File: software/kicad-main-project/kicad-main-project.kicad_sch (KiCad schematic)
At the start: 1 part, among them U1 ESP32-DevKitC

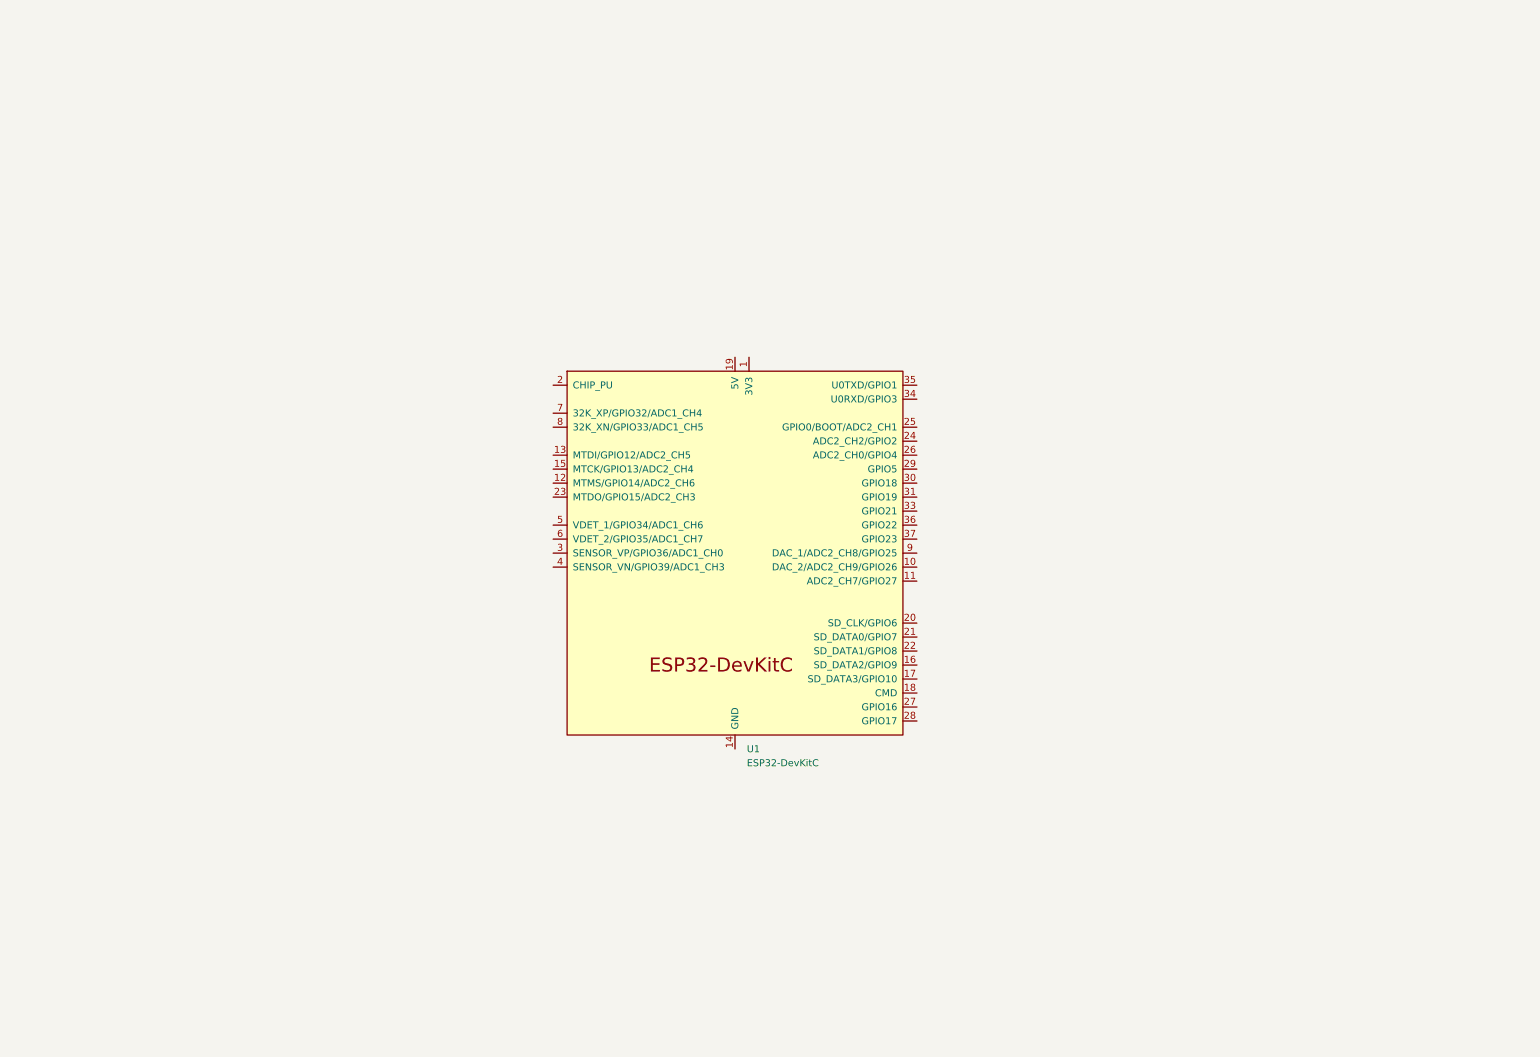
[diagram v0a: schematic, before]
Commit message: update schematic
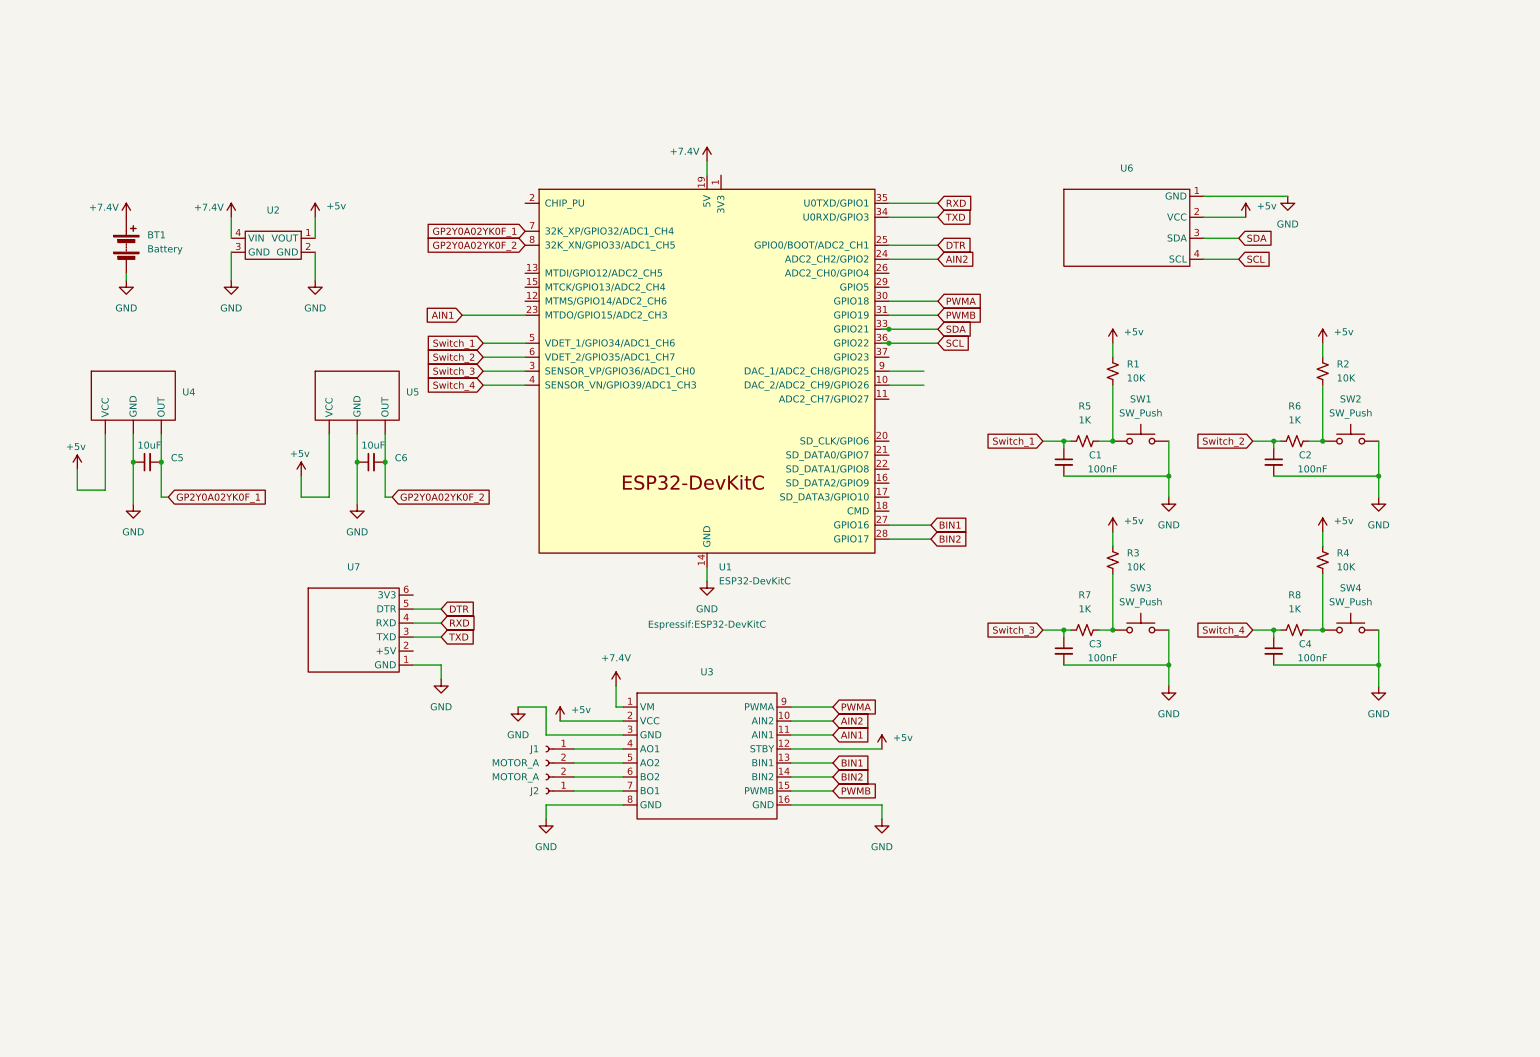
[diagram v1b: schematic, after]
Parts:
- added BT1: Battery, Battery:BatteryHolder_Keystone_1042_1x18650, symbol Device:Battery
- added C1, C2, C3, C4: 100nF, symbol Device:C_Small
- added C5, C6: 10uF, symbol Device:C_Small
- added J1, J2: MOTOR_A, symbol Connector:Conn_01x02_Socket
- added R1, R2, R3, R4: 10K, symbol Device:R_Small_US
- added R5, R6, R7, R8: 1K, symbol Device:R_Small_US
- added SW1, SW2, SW3, SW4: SW_Push, symbol Switch:SW_Push
- added U2: ~, symbol myAMS117-5V-Module:AMS117-5V
- added U3: ~, symbol myTB6612FNG:TB6612_Module
- added U4, U5: ~, symbol myGP2Y0A02YK0F:GP2Y0A02YK0F
- added U6: ~, symbol myLCD_I2C:LCD_I2C
- added U7: ~, symbol myCH340E:CH340E
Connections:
- net GND: now reaches U1.14 (GND), U1.32 (GND), U1.38 (GND)
- net GND: now also BT1.2 (-), C1.2, C2.2, C3.2, C4.2, C5.1, C6.1, SW1.2, SW2.2, SW3.2, SW4.2, U2.2 (GND), U2.3 (GND), U3.16 (GND), U3.3 (GND), U3.8 (GND), U4. (OUT), U5. (OUT), U6.1 (GND), U7.1 (GND)
- net +7.4V: now reaches U1.19 (5V)
- net +7.4V: now also BT1.1 (+), U2.4 (VIN), U3.1 (VM)
- net AIN1: now reaches U1.23 (MTDO/GPIO15/ADC2_CH3)
- net AIN1: now also U3.11 (AIN1)
- net AIN2: now reaches U1.24 (ADC2_CH2/GPIO2)
- net AIN2: now also U3.10 (AIN2)
- net DTR: now reaches U1.25 (GPIO0/BOOT/ADC2_CH1)
- net DTR: now also U7.5 (DTR)
- net BIN1: now reaches U1.27 (GPIO16)
- net BIN1: now also U3.13 (BIN1)
- net BIN2: now reaches U1.28 (GPIO17)
- net BIN2: now also U3.14 (BIN2)
- net Switch_3: now reaches U1.3 (SENSOR_VP/GPIO36/ADC1_CH0)
- net Switch_3: now also C3.1, R7.2
- net PWMA: now reaches U1.30 (GPIO18)
- net PWMA: now also U3.9 (PWMA)
- net PWMB: now reaches U1.31 (GPIO19)
- net PWMB: now also U3.15 (PWMB)
- net SDA: now reaches U1.33 (GPIO21)
- net SDA: now also U6.3 (SDA)
- net TXD: now reaches U1.34 (U0RXD/GPIO3)
- net TXD: now also U7.3 (TXD)
- net RXD: now reaches U1.35 (U0TXD/GPIO1)
- net RXD: now also U7.4 (RXD)
- net SCL: now reaches U1.36 (GPIO22)
- net SCL: now also U6.4 (SCL)
- net Switch_4: now reaches U1.4 (SENSOR_VN/GPIO39/ADC1_CH3)
- net Switch_4: now also C4.1, R8.2
- net Switch_1: now reaches U1.5 (VDET_1/GPIO34/ADC1_CH6)
- net Switch_1: now also C1.1, R5.2
- net Switch_2: now reaches U1.6 (VDET_2/GPIO35/ADC1_CH7)
- net Switch_2: now also C2.1, R6.2
- net GP2Y0A02YK0F_1: now reaches U1.7 (32K_XP/GPIO32/ADC1_CH4)
- net GP2Y0A02YK0F_1: now also C5.2, U4. (OUT)
- net GP2Y0A02YK0F_2: now reaches U1.8 (32K_XN/GPIO33/ADC1_CH5)
- net GP2Y0A02YK0F_2: now also C6.2, U5. (OUT)
- new net: R3.2, R7.1, SW3.1
- new net: R2.2, R6.1, SW2.1
- new net: R1.2, R5.1, SW1.1
- new net: J1.1 (Pin_1), U3.4 (AO1)
- new net: J1.2 (Pin_2), U3.5 (AO2)
- new net: R4.2, R8.1, SW4.1
- new net: J2.1 (Pin_1), U3.7 (BO1)
- new net: J2.2 (Pin_2), U3.6 (BO2)
- new net +5v: R1.1, R2.1, R3.1, R4.1, U2.1 (VOUT), U3.12 (STBY), U3.2 (VCC), U4. (OUT), U5. (OUT), U6.2 (VCC)
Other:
- moved on the sheet: U1

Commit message: update pcb
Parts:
- removed R5, R6, R7, R8: 1K, symbol Device:R_Small_US
- BT1: footprint Battery:BatteryHolder_Keystone_1042_1x18650 -> Connector_JST:JST_XH_S2B-XH-A-1_1x02_P2.50mm_Horizontal
- C1, C2, C3, C4, C5, C6: footprint (none) -> Capacitor_THT:C_Disc_D3.0mm_W1.6mm_P2.50mm
- J1: footprint (none) -> Connector_JST:JST_XH_S2B-XH-A-1_1x02_P2.50mm_Horizontal
- J2: value MOTOR_A -> MOTOR_B; footprint (none) -> Connector_JST:JST_XH_S2B-XH-A-1_1x02_P2.50mm_Horizontal
- R1, R2, R3, R4: footprint (none) -> Resistor_THT:R_Axial_DIN0617_L17.0mm_D6.0mm_P25.40mm_Horizontal
- SW1, SW2, SW3, SW4: footprint (none) -> Button_Switch_THT:SW_PUSH-12mm
- U2: value ~ -> AMS117-5V; footprint (none) -> myAMS117-5V:Untitled
- U3: value ~ -> TB6612FNG; footprint (none) -> myTB6612FNG:Untitled
- U4: value ~ -> GP2Y0A02YK0F_1; footprint (none) -> Connector_JST:JST_XH_S3B-XH-A-1_1x03_P2.50mm_Horizontal
- U5: value ~ -> GP2Y0A02YK0F_2; footprint (none) -> Connector_JST:JST_XH_S3B-XH-A-1_1x03_P2.50mm_Horizontal
- U6: value ~ -> LCD-I2C; footprint (none) -> Connector_JST:JST_XH_S4B-XH-A_1x04_P2.50mm_Horizontal
- U7: value ~ -> CH340E; footprint (none) -> myCH340e:Untitled
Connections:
- net Switch_1 is gone; now on net Button_1: C1.1, U1.5 (VDET_1/GPIO34/ADC1_CH6)
- net Switch_2 is gone; now on net Button_2: C2.1, U1.6 (VDET_2/GPIO35/ADC1_CH7)
- net Switch_3 is gone; now on net Button_3: C3.1, U1.3 (SENSOR_VP/GPIO36/ADC1_CH0)
- net Switch_4 is gone; now on net Button_4: C4.1, U1.4 (SENSOR_VN/GPIO39/ADC1_CH3)
- net +5v: now also U4.3 (VCC), U5.3 (VCC); no longer U4. (OUT), U5. (OUT)
- net GND: now also U4.2 (GND), U5.2 (GND); no longer U4. (OUT), U5. (OUT)
- net GP2Y0A02YK0F_1: now also U4.1 (OUT); no longer U4. (OUT)
- net GP2Y0A02YK0F_2: now also U5.1 (OUT); no longer U5. (OUT)
- net Button_3: now reaches R3.2, SW3.1
- net Button_2: now reaches R2.2, SW2.1
- net Button_1: now reaches R1.2, SW1.1
- net Button_4: now reaches R4.2, SW4.1
- no-connect marks 0 -> 7
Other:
- note added: "KHỐI LCD I2C"
- moved on the sheet: BT1, C1, C2, C3, C4, C5, C6, J1, J2, R1, R2, R3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

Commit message: update gerber + bom + image_
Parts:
- removed C5, C6: 10uF, Capacitor_THT:C_Disc_D3.0mm_W1.6mm_P2.50mm, symbol Device:C_Small
- removed U7: CH340E, myCH340e:Untitled, symbol myCH340E:CH340E
- added U10: K6-FALL-3, Connector_JST:JST_XH_S3B-XH-A-1_1x03_P2.50mm_Horizontal, symbol myK6-Fall:K6-Fall
- added U7: K6-FALL-1, Connector_JST:JST_XH_S3B-XH-A-1_1x03_P2.50mm_Horizontal, symbol myK6-Fall:K6-Fall
- added U8: AMS117-1.2V, myAMS117-5V:Untitled, symbol myAMS117-1V2-Module:myAMS117-1V2
- added U9: K6-FALL-2, Connector_JST:JST_XH_S3B-XH-A-1_1x03_P2.50mm_Horizontal, symbol myK6-Fall:K6-Fall
- R1, R2, R3, R4: footprint Resistor_THT:R_Axial_DIN0617_L17.0mm_D6.0mm_P25.40mm_Horizontal -> Resistor_THT:R_Axial_DIN0204_L3.6mm_D1.6mm_P2.54mm_Vertical
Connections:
- net +7.4V: now also U8.4 (VIN)
- net GND: now also U10.3 (GND), U7.3 (GND), U8.2 (GND), U8.3 (GND), U9.3 (GND)
- net K6-Fall-2: now reaches U1.10 (DAC_2/ADC2_CH9/GPIO26)
- net K6-Fall-2: now also U9.2 (OUT)
- net K6-Fall-3: now reaches U1.11 (ADC2_CH7/GPIO27)
- net K6-Fall-3: now also U10.2 (OUT)
- net K6-Fall-1: now reaches U1.9 (DAC_1/ADC2_CH8/GPIO25)
- net K6-Fall-1: now also U7.2 (OUT)
- new net +1.2v: U10.1 (VCC), U7.1 (VCC), U8.1 (VOUT), U9.1 (VCC)
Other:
- note removed: "KHỐI LCD I2C"
- moved on the sheet: BT1, C1, C2, C3, C4, J1, J2, R1, R2, R3, R4, SW1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
